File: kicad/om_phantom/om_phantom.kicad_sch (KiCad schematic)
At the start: 22 parts, among them J1 VIN, J2 GND, J3 EN, J4 VOUT, J5 GND, U1 TPS61391, U2 TPS7A4101

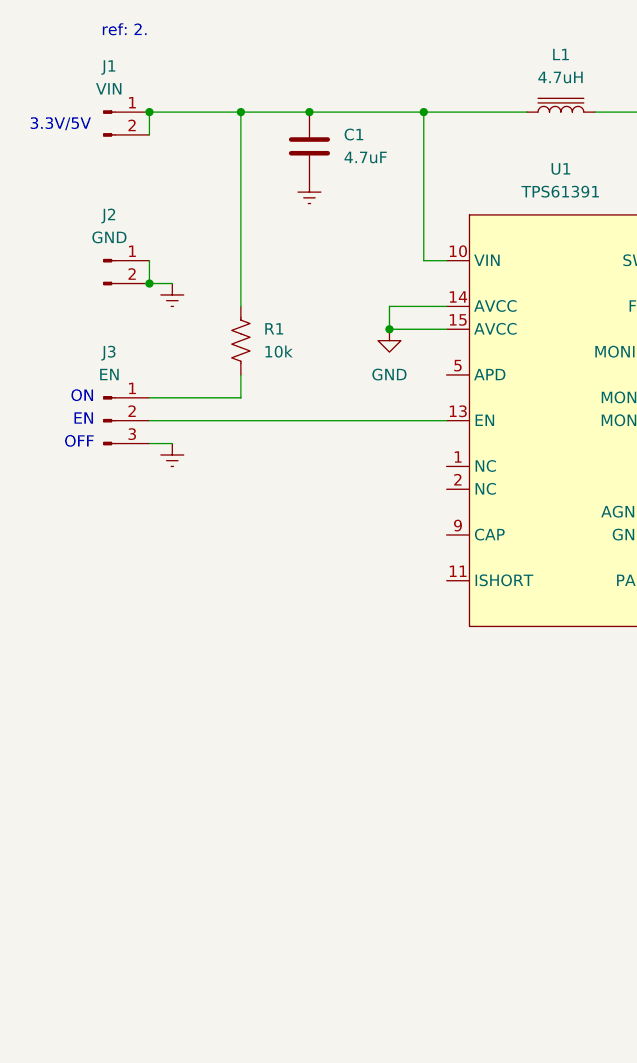
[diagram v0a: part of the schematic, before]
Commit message: phantom switch (#6)
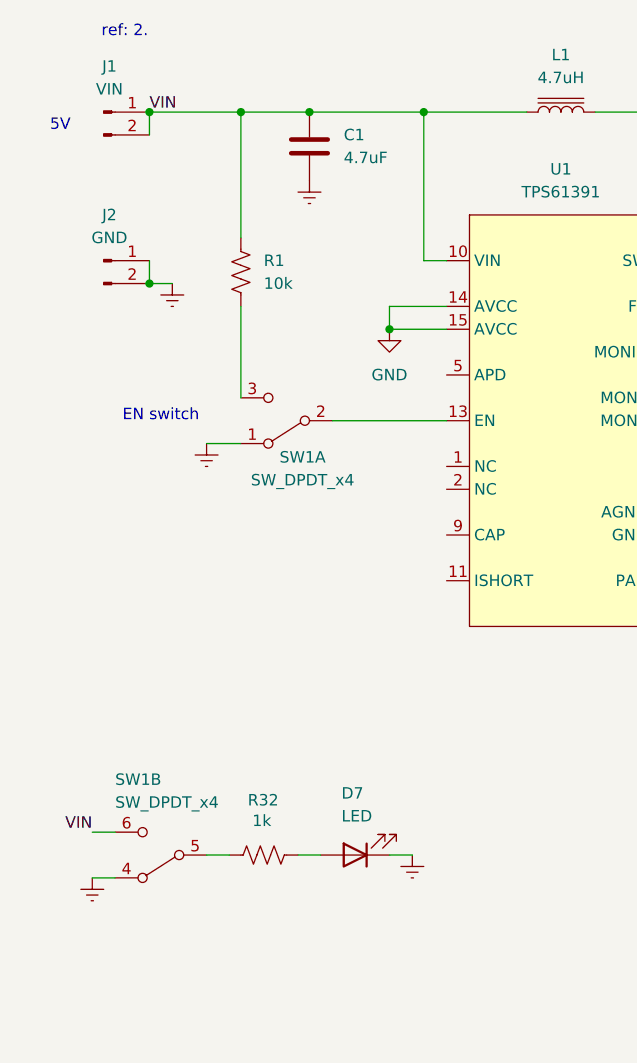
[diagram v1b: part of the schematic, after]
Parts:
- removed J3: EN, symbol Connector:Conn_01x03_Pin
- added D7: LED, symbol Device:LED
- added R32: 1k, symbol Device:R_US
- added SW1: SW_DPDT_x4, symbol openmic:SW_DPDT_x2
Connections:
- net Earth: now also D7.1 (K), SW1.1 (A), SW1.4 (A)
- net VIN: now reaches C1.1, J1.1 (Pin_1), J1.2 (Pin_2), L1.1, R1.1, U1.10 (VIN)
- net VIN: now also SW1.6 (C)
- net at R1.2: now also SW1.3 (C)
- net at U1.13 (EN): now also SW1.2 (B)
- new net: R32.1, SW1.5 (B)
- new net: D7.2 (A), R32.2
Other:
- note added: "5V"
- note added: "EN switch"
- note removed: "3.3V/5V"
- note removed: "EN"
- note removed: "OFF"
- note removed: "ON"
- moved on the sheet: R1
